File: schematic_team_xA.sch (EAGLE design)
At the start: 31 parts, among them U1 ATMEGA328P-AU, U2 MPU-6050

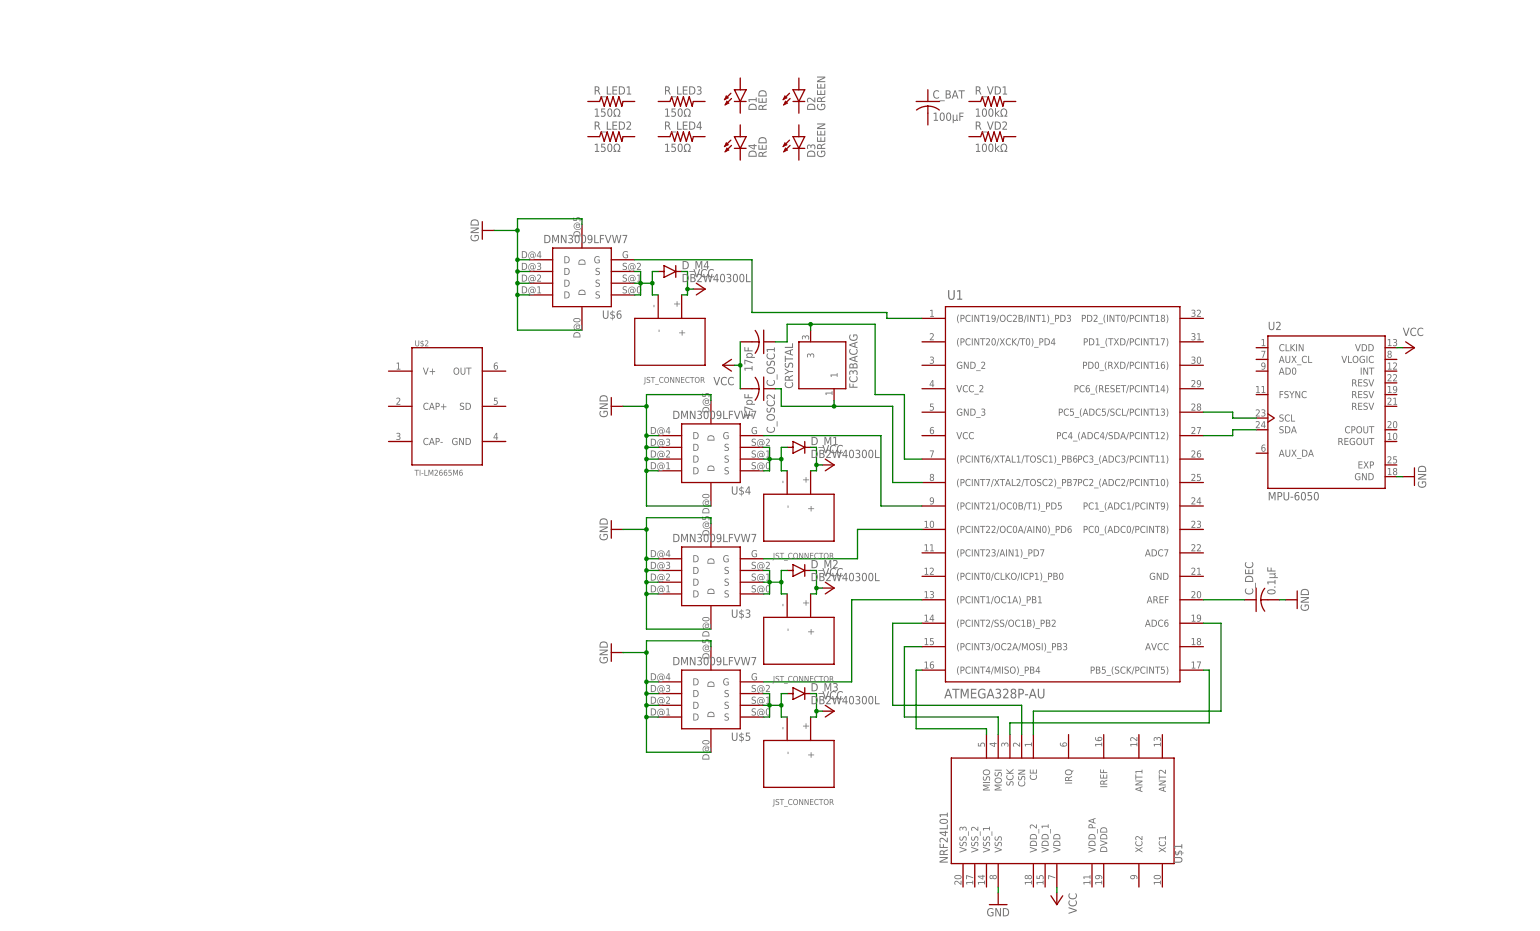
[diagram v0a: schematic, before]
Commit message: LED Schematic + Battery
Wired the LEDs on the symbol schematic and connected the battery. Still no chargepump
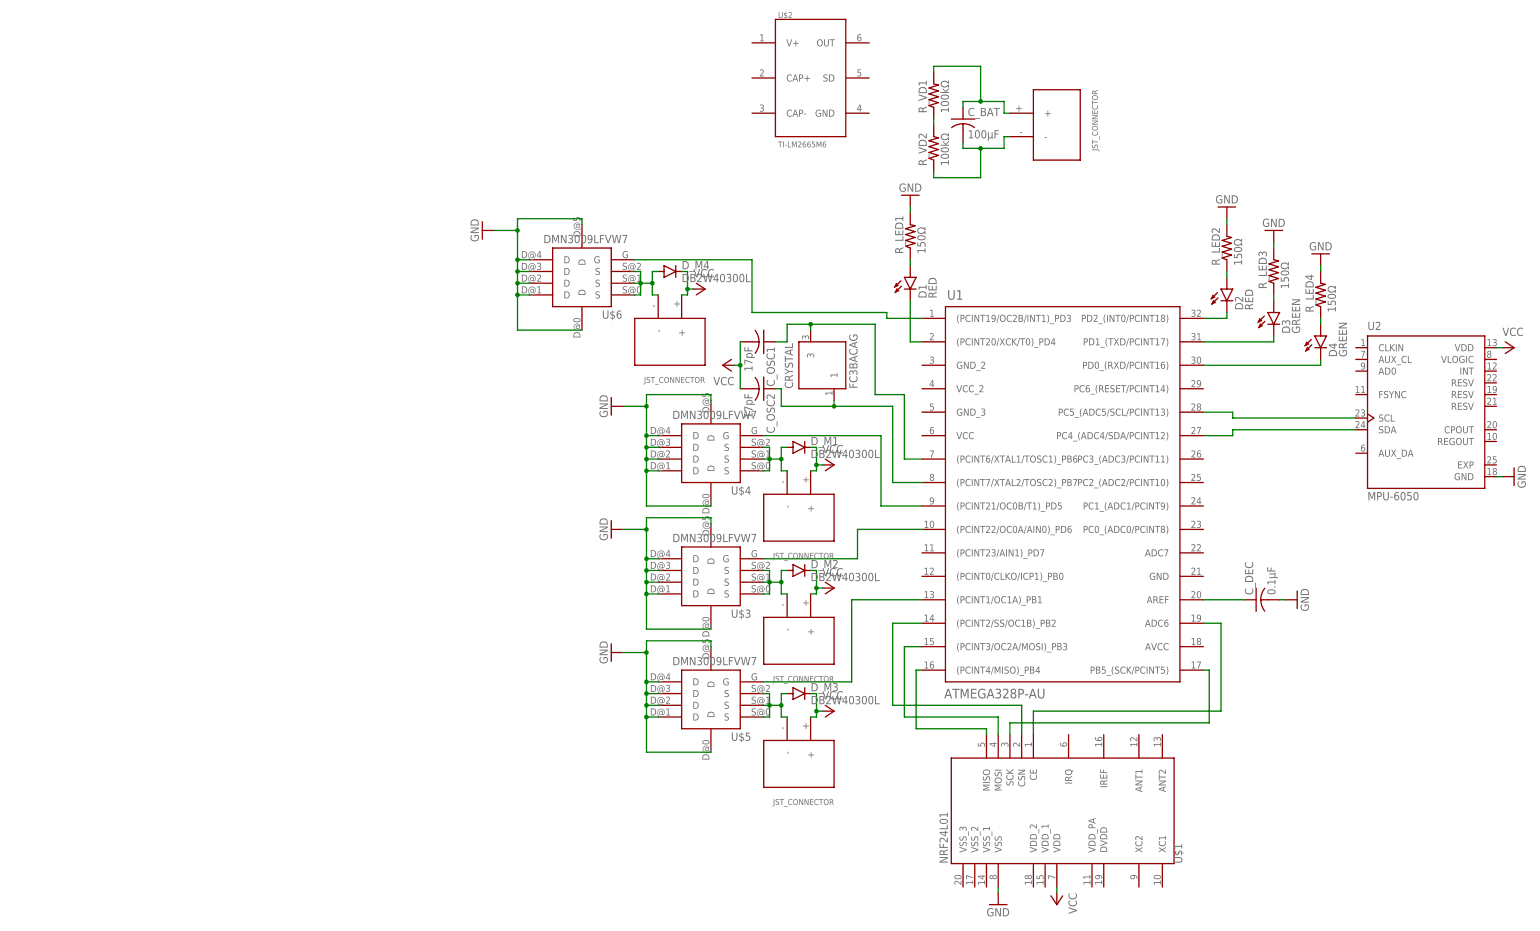
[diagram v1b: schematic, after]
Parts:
- added MOTOR5: JST_CONNECTOR_FEMALE, quad:JST_CONNECTOR_FEMALE
- D2: value GREEN -> RED; device LEDs:LED-GREEN0603 -> LEDs:LED-RED0603
- D4: value RED -> GREEN; device LEDs:LED-RED0603 -> LEDs:LED-GREEN0603
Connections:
- new net N$14: C_BAT.1, MOTOR5.+, R_VD1.2
- new net N$20: C_BAT.2, MOTOR5.-, R_VD2.1
- new net N$21: D1.A, R_LED1.1
- new net N$22: D2.A, R_LED2.1
- new net N$23: R_VD1.1, R_VD2.2
- new net N$24: D3.A, R_LED3.1
- new net N$25: D4.A, R_LED4.1
- new net N$26: D1.C, U1.(PCINT20/XCK/T0)_PD4
- new net N$27: D2.C, U1.PD2_(INT0/PCINT18)
- new net N$28: D3.C, U1.PD1_(TXD/PCINT17)
- new net N$29: D4.C, U1.PD0_(RXD/PCINT16)
- net GND: now also R_LED1.2, R_LED2.2, R_LED3.2, R_LED4.2
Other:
- moved on the sheet: C_BAT, D1, D2, D3, D4, R_LED1, R_LED2, R_LED3, R_LED4, R_VD1, R_VD2, U$2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

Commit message: Wired chargepump
Wired the charge pump to the symbol schematic and added the capacitors and battery (jst junction for now).
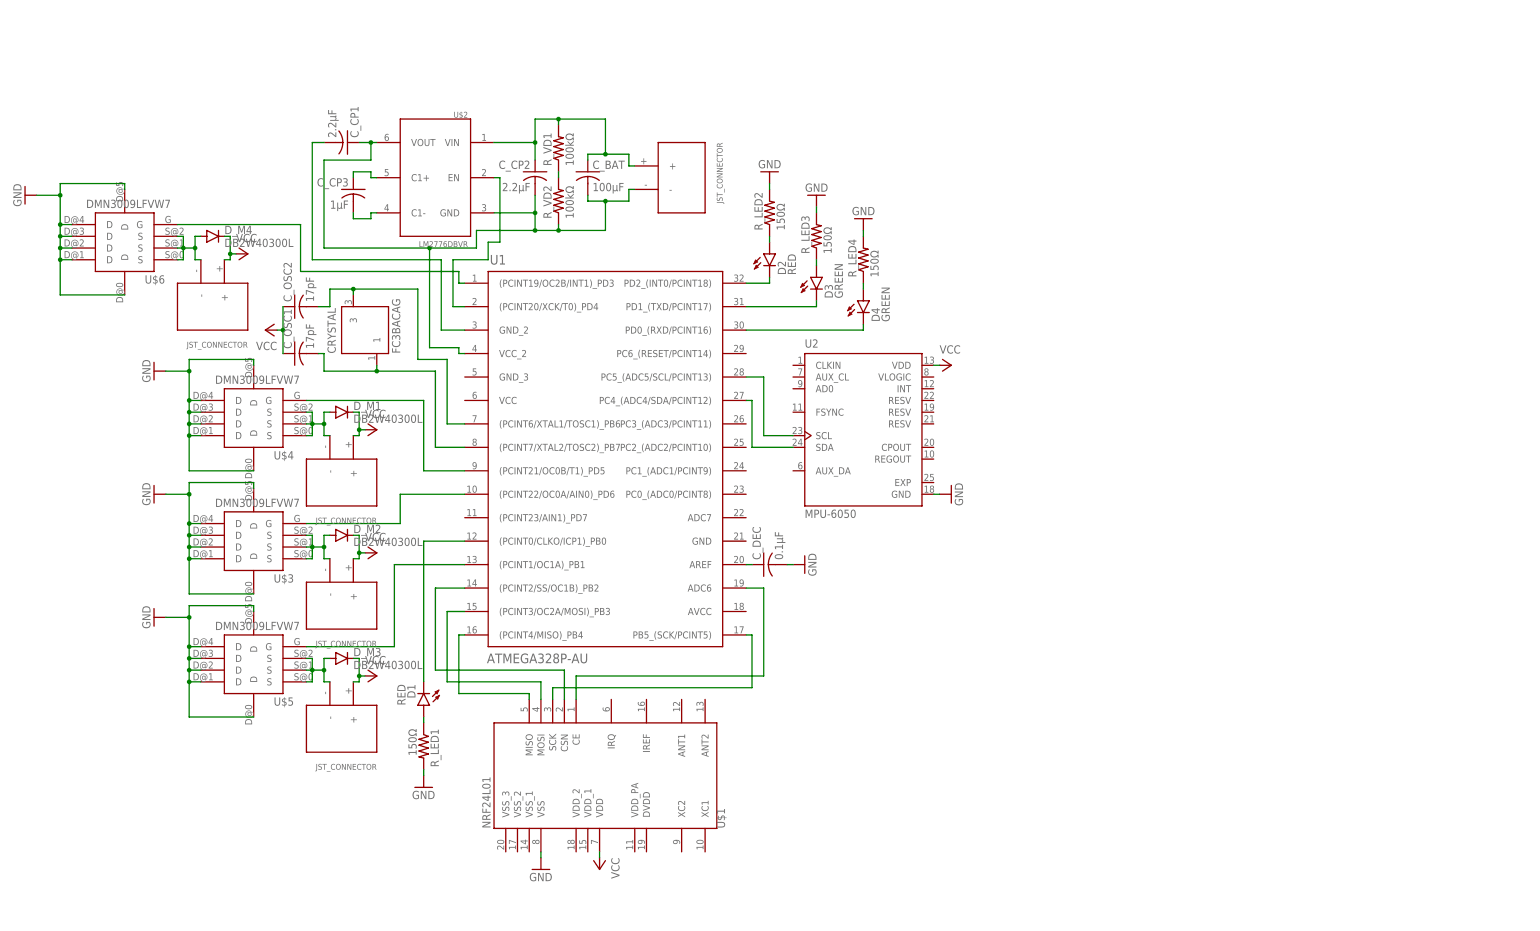
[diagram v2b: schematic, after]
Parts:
- added C_CP1, C_CP2: 2.2μF, rcl:C-USC0603
- added C_CP3: 1μF, rcl:C-USC0603
- C_OSC1, C_OSC2: device resistor:C-USC0805 -> rcl:C-USC0402
- U$2: value TI-LM2665M6 -> LM2776DBVR; device TI-LM2665M6:TI-LM2665M6 -> LM2776:LM2776DBVR
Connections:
- new net N$30: C_CP3.1, U$2.C1+
- new net N$31: C_CP3.2, U$2.C1-
- new net N$32: C_BAT.2, C_CP1.1, C_CP2.2, MOTOR5.-, R_VD2.1, U$2.GND, U$2.VOUT, U1.VCC_2
- new net N$34: D1.C, U1.(PCINT0/CLKO/ICP1)_PB0
- net N$14: now also C_CP2.1, U$2.VIN
- net N$2: now also C_OSC1.2; no longer C_OSC2.1
- net N$20: now also C_CP1.2, U1.GND_2; no longer C_BAT.2, MOTOR5.-, R_VD2.1
- net N$26: now also U$2.EN; no longer D1.C
- net N$9: now also C_OSC2.2; no longer C_OSC1.1
- net VCC: now also C_OSC1.1, C_OSC2.1; no longer C_OSC1.2, C_OSC2.2
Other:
- moved on the sheet: CRYSTAL, C_BAT, C_DEC, C_OSC1, C_OSC2, D1, D2, D3, D4, D_M1, D_M2, D_M3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
